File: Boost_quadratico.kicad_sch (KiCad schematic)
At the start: 10 parts

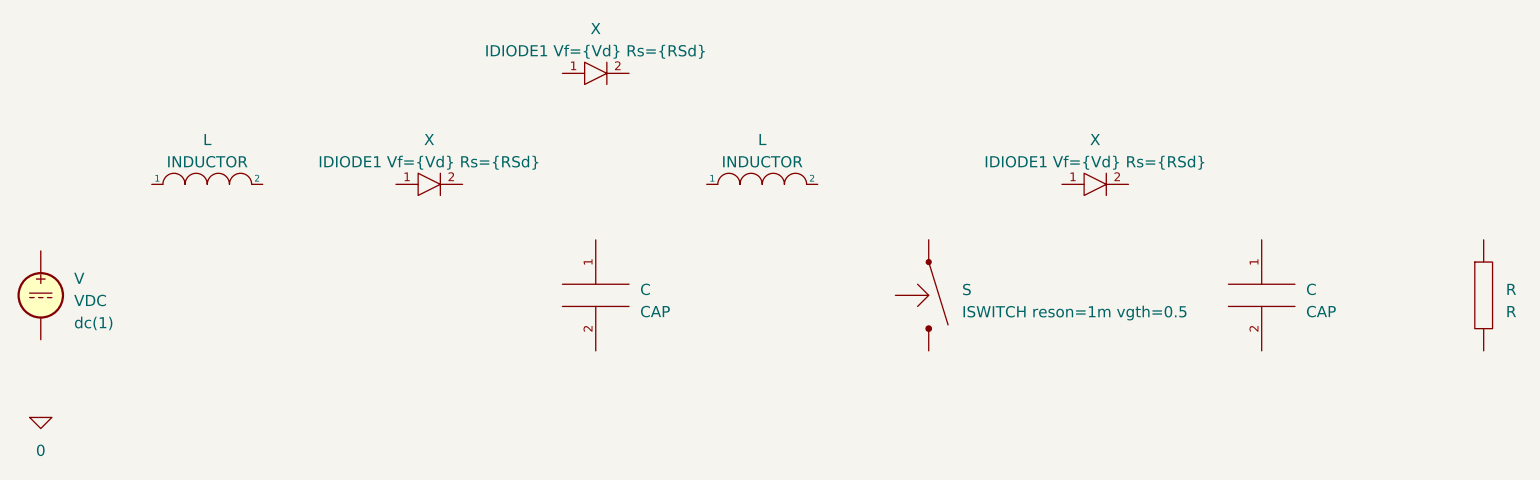
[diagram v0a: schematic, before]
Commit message: Circuito comutado roteado
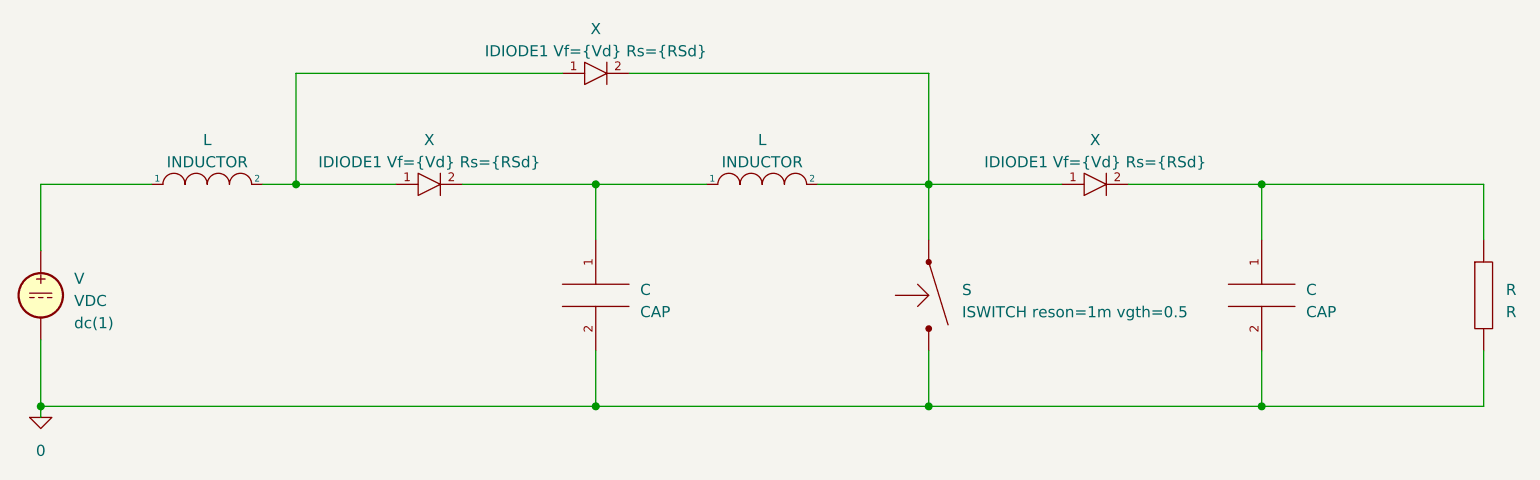
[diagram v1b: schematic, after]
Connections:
- net 0: now also C.2, C.2, R.2, S.3 (S), V.2
- net at V.1: now also L.1
- net at L.1: now also C.1, X.2
- net at L.2: now also S.1 (D), X.1, X.2
- net at X.1: now also L.2, X.1
- net at X.2: now also C.1, R.1
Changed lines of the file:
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@@
 (kicad_sch (version 20220404) (generator eeschema)
   (paper "A4")
+  (junction (at 54.61 88.9) (diameter 0) (color 0 0 0 0)
+  )
+  (junction (at 165.1 114.3) (diameter 0) (color 0 0 0 0)
+  )
+  (junction (at 88.9 114.3) (diameter 0) (color 0 0 0 0)
+  )
+  (junction (at 127 88.9) (diameter 0) (color 0 0 0 0)
+  )
+  (junction (at 88.9 88.9) (diameter 0) (color 0 0 0 0)
+  )
+  (junction (at 165.1 88.9) (diameter 0) (color 0 0 0 0)
+  )
+  (junction (at 127 114.3) (diameter 0) (color 0 0 0 0)
+  )
+  (junction (at 25.4 114.3) (diameter 0) (color 0 0 0 0)
+  )
+  (wire (pts (xy 127 88.9) (xy 142.24 88.9))
+    (stroke (width 0) (type default))
+  )
+  (wire (pts (xy 165.1 114.3) (xy 190.5 114.3))
+    (stroke (width 0) (type default))
+  )
+  (wire (pts (xy 92.71 76.2) (xy 127 76.2))
+    (stroke (width 0) (type default))
+  )
+  (wire (pts (xy 190.5 95.25) (xy 190.5 88.9))
+    (stroke (width 0) (type default))
+  )
+  (wire (pts (xy 114.3 88.9) (xy 127 88.9))
+    (stroke (width 0) (type default))
+  )
+  (wire (pts (xy 25.4 88.9) (xy 38.1 88.9))
+    (stroke (width 0) (type default))
+  )
+  (wire (pts (xy 190.5 107.95) (xy 190.5 114.3))
+    (stroke (width 0) (type default))
+  )
+  (wire (pts (xy 127 114.3) (xy 165.1 114.3))
+    (stroke (width 0) (type default))
+  )
+  (wire (pts (xy 50.8 88.9) (xy 54.61 88.9))
+    (stroke (width 0) (type default))
+  )
+  (wire (pts (xy 73.66 88.9) (xy 88.9 88.9))
+    (stroke (width 0) (type default))
+  )
+  (wire (pts (xy 85.09 76.2) (xy 54.61 76.2))
+    (stroke (width 0) (type default))
+  )
+  (wire (pts (xy 127 114.3) (xy 88.9 114.3))
+    (stroke (width 0) (type default))
+  )
+  (wire (pts (xy 127 107.95) (xy 127 114.3))
+    (stroke (width 0) (type default))
+  )
+  (wire (pts (xy 54.61 88.9) (xy 66.04 88.9))
+    (stroke (width 0) (type default))
+  )
+  (wire (pts (xy 54.61 76.2) (xy 54.61 88.9))
+    (stroke (width 0) (type default))
+  )
+  (wire (pts (xy 190.5 88.9) (xy 165.1 88.9))
+    (stroke (width 0) (type default))
+  )
+  (wire (pts (xy 127 76.2) (xy 127 88.9))
+    (stroke (width 0) (type default))
+  )
+  (wire (pts (xy 149.86 88.9) (xy 165.1 88.9))
+    (stroke (width 0) (type default))
+  )
+  (wire (pts (xy 165.1 107.95) (xy 165.1 114.3))
+    (stroke (width 0) (type default))
+  )
+  (wire (pts (xy 25.4 106.68) (xy 25.4 114.3))
+    (stroke (width 0) (type default))
+  )
+  (wire (pts (xy 25.4 96.52) (xy 25.4 88.9))
+    (stroke (width 0) (type default))
+  )
+  (wire (pts (xy 88.9 88.9) (xy 88.9 95.25))
+    (stroke (width 0) (type default))
+  )
+  (wire (pts (xy 88.9 114.3) (xy 88.9 107.95))
+    (stroke (width 0) (type default))
+  )
+  (wire (pts (xy 88.9 88.9) (xy 101.6 88.9))
+    (stroke (width 0) (type default))
+  )
+  (wire (pts (xy 127 88.9) (xy 127 95.25))
+    (stroke (width 0) (type default))
+  )
+  (wire (pts (xy 25.4 114.3) (xy 25.4 115.57))
+    (stroke (width 0) (type default))
+  )
+  (wire (pts (xy 165.1 88.9) (xy 165.1 95.25))
+    (stroke (width 0) (type default))
+  )
+  (wire (pts (xy 25.4 114.3) (xy 88.9 114.3))
+    (stroke (width 0) (type default))
+  )
   (symbol (lib_id "Simulation_SPICE:VDC") (at 25.4 101.6 0) (unit 1)
     (in_bom yes) (on_board yes) (fields_autoplaced)

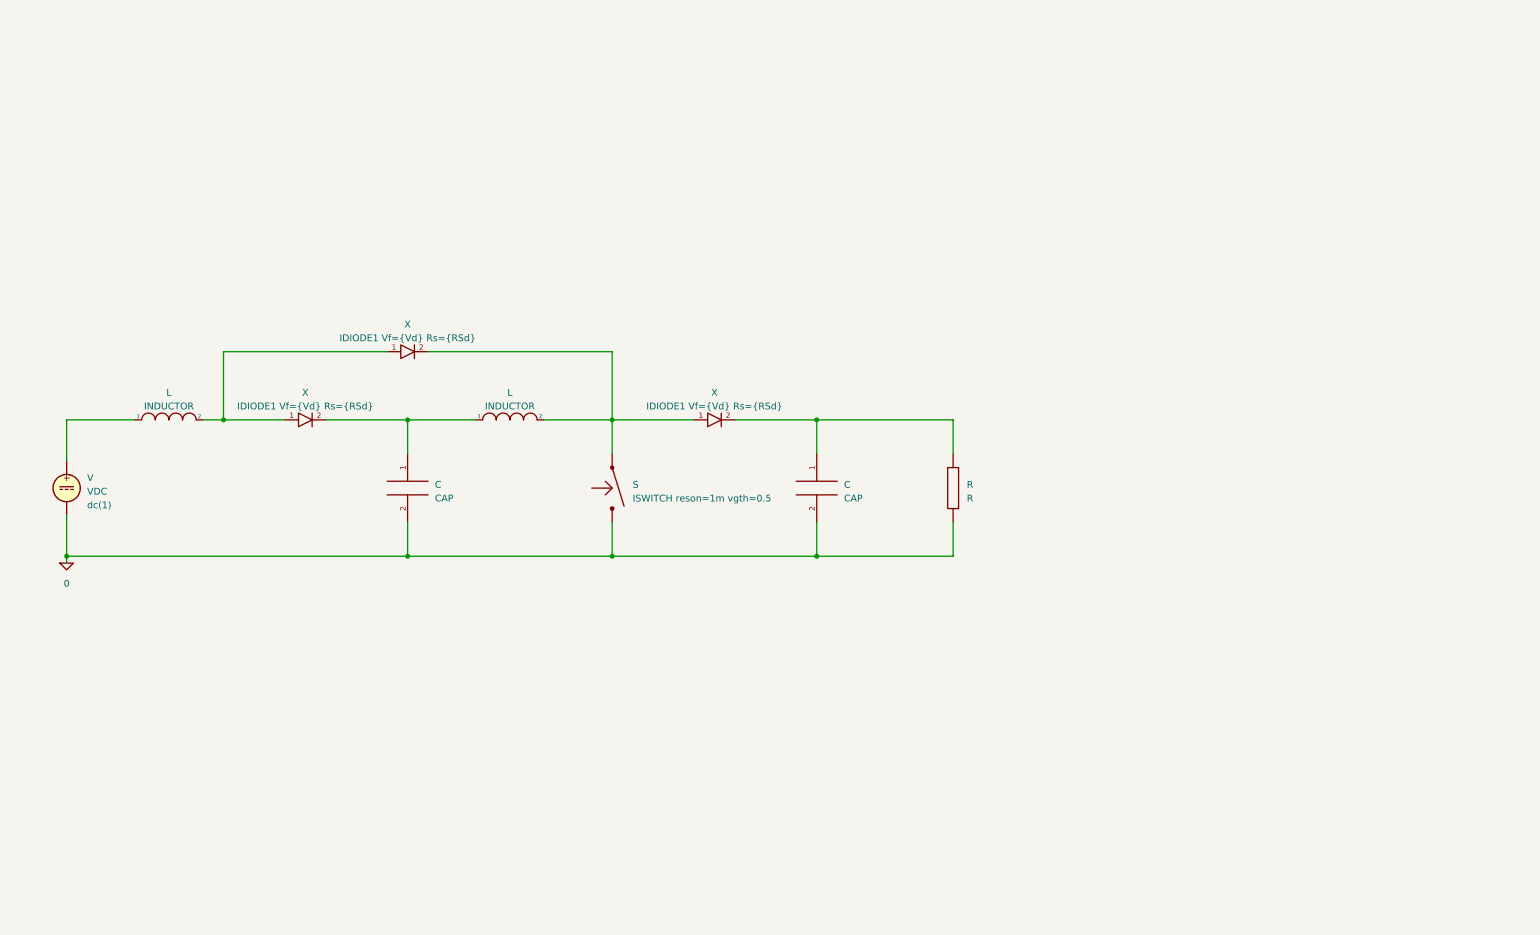
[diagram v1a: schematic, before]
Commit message: Modelo médio PWMgst
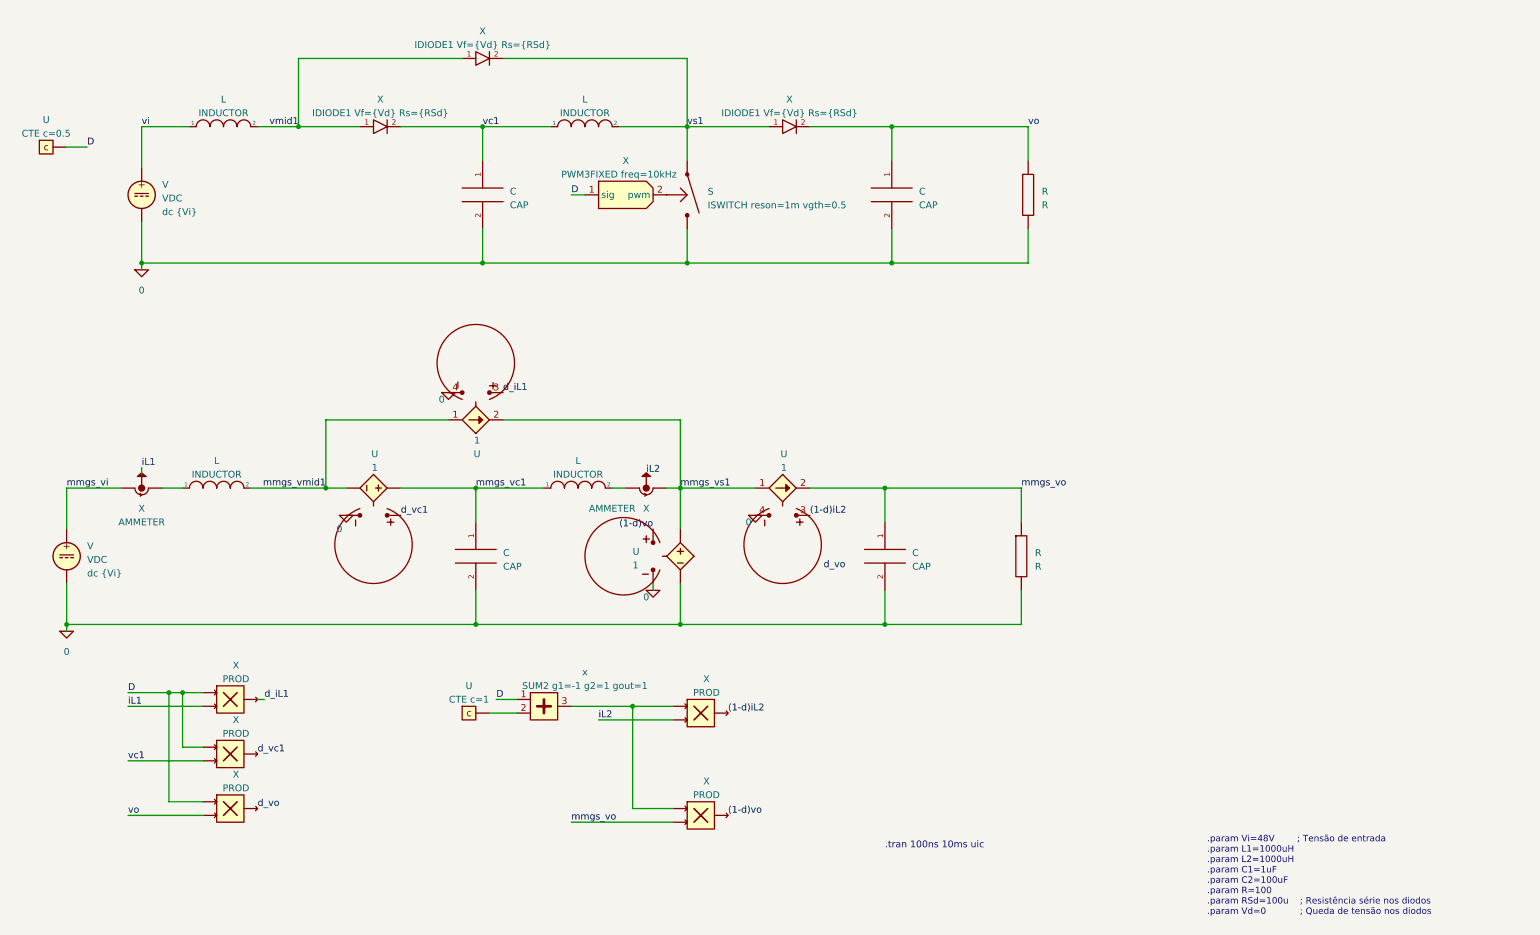
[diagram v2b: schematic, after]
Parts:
- added C (x2): CAP, symbol pspice:CAP
- added L (x2): INDUCTOR, symbol pspice:INDUCTOR
- added R: R, symbol pspice:R
- added U (x2): VCCS, symbol power electronics:VCCS
- added U (x2): VCVS, symbol power electronics:VCVS
- added V: VDC, symbol Simulation_SPICE:VDC
- added X (x5): product, symbol Signal Processing:product
- added X: PWM3_FIXED, symbol power electronics:PWM3_FIXED
- added X (x2): Ammeter Compact, symbol Signal Processing:Ammeter Compact
- added x: sum2, symbol Signal Processing:sum2
- V: Spice_Model dc(1) -> dc {Vi}
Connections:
- net 0: now also C.2, C.2, R.2, U.2, U.4, U.4, U.4, U.4, V.2
- net vi: now reaches L.1, V.1
- net vc1: now reaches C.1, L.1, X.2
- net vc1: now also X.2
- net vs1: now reaches L.2, S.1 (D), X.1, X.2
- net vmid1: now reaches L.2, X.1, X.1
- net at S.2 (G): now also X.2 (pwm)
- net vo: now reaches C.1, R.1, X.2
- net vo: now also X.2
- new net: X.1, X.1, x.3
- new net: L.2, X.1
- new net: L.1, X.2
- new net (1-d)iL2: U.3, X.3
- new net (1-d)vo: U.3, X.3
- new net D: X.1, X.1, X.1, X.1 (sig), x.1
- new net d_iL1: U.3, X.3
- new net d_vc1: U.3, X.3
- new net d_vo: X.3
- new net iL1: X.2, X.3
- new net iL2: X.2, X.3
- new net mmgs_vc1: C.1, L.1, U.1
- new net mmgs_vi: V.1, X.1
- new net mmgs_vmid1: L.2, U.1, U.2
- new net mmgs_vo: C.1, R.1, U.2, X.2
- new net mmgs_vs1: U.1, U.1, U.2, X.2
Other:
- note added: ".param Vi=48V ; Tensão de entrada .param L1=1000uH .param L2=1000uH .param C1=1uF .param C2=100uF .param R=100 .param RSd=100u ; Resistência série nos diodos .param Vd=0 ; Queda de tensão nos diodos"
- note added: ".tran 100ns 10ms uic"
- company: (none) -> INEP - UFSC
- title: (none) -> Conversor Boost Quadrático
- moved on the sheet: C, L, R, S, V, X

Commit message: Modelo médio feito, mas oscilando demais
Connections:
- net (1-d)iL2: no longer U.3
- net (1-d)vo: no longer U.3
- net 0: now also U.2, U.3; no longer U.2, U.4
- net d_iL1: now also U.4
- net d_vo: now also U.3
- net mmgs_vo: now also U.1; no longer U.2
- net mmgs_vs1: now also U.2; no longer U.1
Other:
- moved on the sheet: U
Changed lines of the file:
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@@
+    (stroke (width 0) (type default))
+  )
+  (wire (pts (xy 68.58 34.29) (xy 80.01 34.29))
+    (stroke (width 0) (type default))
+  )
+  (wire (pts (xy 68.58 21.59) (xy 68.58 34.29))
+    (stroke (width 0) (type default))
+  )
+  (wire (pts (xy 104.14 143.51) (xy 109.22 143.51))
+    (stroke (width 0) (type default))
+  )
+  (wire (pts (xy 50.8 160.02) (xy 44.45 160.02))
+    (stroke (width 0) (type default))
+  )
+  (wire (pts (xy 36.83 142.24) (xy 50.8 142.24))
+    (stroke (width 0) (type default))
+  )
+  (wire (pts (xy 204.47 34.29) (xy 179.07 34.29))
+    (stroke (width 0) (type default))
+  )
+  (wire (pts (xy 177.8 101.6) (xy 177.8 107.95))
+    (stroke (width 0) (type default))
+  )
+  (wire (pts (xy 25.4 127) (xy 101.6 127))
+    (stroke (width 0) (type default))
+  )
+  (wire (pts (xy 140.97 21.59) (xy 140.97 34.29))
+    (stroke (width 0) (type default))
+  )
+  (wire (pts (xy 163.83 34.29) (xy 179.07 34.29))
+    (stroke (width 0) (type default))
+  )
+  (wire (pts (xy 36.83 152.4) (xy 50.8 152.4))
     (stroke (width 0) (type default))
   )
   (wire (pts (xy 134.62 119.38) (xy 134.62 120.65))
-    (stroke (width 0) (type default))
-  )
-  (wire (pts (xy 68.58 34.29) (xy 80.01 34.29))
-    (stroke (width 0) (type default))
-  )
-  (wire (pts (xy 68.58 21.59) (xy 68.58 34.29))
-    (stroke (width 0) (type default))
-  )
-  (wire (pts (xy 104.14 143.51) (xy 109.22 143.51))
-    (stroke (width 0) (type default))
-  )
-  (wire (pts (xy 50.8 160.02) (xy 44.45 160.02))
-    (stroke (width 0) (type default))
-  )
-  (wire (pts (xy 36.83 142.24) (xy 50.8 142.24))
-    (stroke (width 0) (type default))
-  )
-  (wire (pts (xy 204.47 34.29) (xy 179.07 34.29))
-    (stroke (width 0) (type default))
-  )
-  (wire (pts (xy 177.8 101.6) (xy 177.8 107.95))
-    (stroke (width 0) (type default))
-  )
-  (wire (pts (xy 25.4 127) (xy 101.6 127))
-    (stroke (width 0) (type default))
-  )
-  (wire (pts (xy 140.97 21.59) (xy 140.97 34.29))
-    (stroke (width 0) (type default))
-  )
-  (wire (pts (xy 163.83 34.29) (xy 179.07 34.29))
-    (stroke (width 0) (type default))
-  )
-  (wire (pts (xy 36.83 152.4) (xy 50.8 152.4))
     (stroke (width 0) (type default))
   )
@@
     (effects (font (size 1.27 1.27)) (justify left bottom))
   )
-  (label "(1-d)vo" (at 134.62 109.22 0) (fields_autoplaced)
-    (effects (font (size 1.27 1.27)) (justify right bottom))
+  (label "d_vo" (at 163.83 96.52 0) (fields_autoplaced)
+    (effects (font (size 1.27 1.27)) (justify left bottom))
   )
   (label "d_iL1" (at 106.68 83.82 0) (fields_autoplaced)
@@
     (effects (font (size 1.27 1.27)) (justify left bottom))
   )
-  (label "(1-d)iL2" (at 163.83 106.68 0) (fields_autoplaced)
+  (label "d_iL1" (at 134.62 109.22 0) (fields_autoplaced)
     (effects (font (size 1.27 1.27)) (justify left bottom))
   )
@@
     (pin "2")
   )
-  (symbol (lib_id "power electronics:VCVS") (at 139.7 114.3 0) (mirror y) (unit 1)
+  (symbol (lib_id "power electronics:VCVS") (at 158.75 101.6 270) (mirror x) (unit 1)
     (in_bom no) (on_board no)
     (default_instance (reference "U") (unit 1) (value "VCVS") (footprint ""))
-    (property "Reference" "U" (id 0) (at 130.81 113.4297 0)
+    (property "Reference" "U" (id 0) (at 159.6203 92.71 0)
       (effects (font (size 1.27 1.27)) (justify right))
     )
-    (property "Value" "VCVS" (id 1) (at 139.7 132.08 0)
-      (effects (font (size 1.27 1.27)) hide)
-    )
-    (property "Footprint" "" (id 2) (at 139.7 129.54 0)
-      (effects (font (size 1.27 1.27)) hide)
-    )
-    (property "Datasheet" "" (id 3) (at 139.7 129.54 0)
-      (effects (font (size 1.27 1.27)) hide)
-    )
-    (property "Spice_Primitive" "E" (id 4) (at 139.7 127 0)
-      (effects (font (size 1.27 1.27)) hide)
-    )
-    (property "Spice_Model" "1" (id 5) (at 130.81 115.9697 0)
+    (property "Value" "VCVS" (id 1) (at 140.97 101.6 0)
+      (effects (font (size 1.27 1.27)) hide)
+    )
+    (property "Footprint" "" (id 2) (at 143.51 101.6 0)
+      (effects (font (size 1.27 1.27)) hide)
+    )
+    (property "Datasheet" "" (id 3) (at 143.51 101.6 0)
+      (effects (font (size 1.27 1.27)) hide)
+    )
+    (property "Spice_Primitive" "E" (id 4) (at 146.05 101.6 0)
+      (effects (font (size 1.27 1.27)) hide)
+    )
+    (property "Spice_Model" "1" (id 5) (at 157.0803 92.71 0)
       (effects (font (size 1.27 1.27)) (justify right))
     )
-    (property "Spice_Netlist_Enabled" "Y" (id 6) (at 139.7 129.54 0)
+    (property "Spice_Netlist_Enabled" "Y" (id 6) (at 143.51 101.6 0)
       (effects (font (size 1.27 1.27)) hide)
     )
@@
     (pin "3")
   )
-  (symbol (lib_id "power electronics:VCCS") (at 158.75 101.6 270) (unit 1)
+  (symbol (lib_id "power electronics:VCCS") (at 139.7 114.3 180) (unit 1)
     (in_bom no) (on_board no) (fields_autoplaced)
     (default_instance (reference "U") (unit 1) (value "VCCS") (footprint ""))
-    (property "Reference" "U" (id 0) (at 158.9853 95.25 90)
-      (effects (font (size 1.27 1.27)))
-    )
-    (property "Value" "VCCS" (id 1) (at 139.7 101.6 0)
-      (effects (font (size 1.27 1.27)) hide)
-    )
-    (property "Footprint" "" (id 2) (at 143.51 101.6 0)
-      (effects (font (size 1.27 1.27)) hide)
-    )
-    (property "Datasheet" "" (id 3) (at 143.51 101.6 0)
-      (effects (font (size 1.27 1.27)) hide)
-    )
-    (property "Spice_Primitive" "G" (id 4) (at 144.78 101.6 0)
-      (effects (font (size 1.27 1.27)) hide)
-    )
-    (property "Spice_Model" "1" (id 5) (at 158.9853 97.79 90)
-      (effects (font (size 1.27 1.27)))
-    )
-    (property "Spice_Netlist_Enabled" "Y" (id 6) (at 142.24 101.6 0)
+    (property "Reference" "U" (id 0) (at 143.51 113.9003 0)
+      (effects (font (size 1.27 1.27)) (justify right))
+    )
+    (property "Value" "VCCS" (id 1) (at 139.7 95.25 0)
+      (effects (font (size 1.27 1.27)) hide)
+    )
+    (property "Footprint" "" (id 2) (at 139.7 99.06 0)
+      (effects (font (size 1.27 1.27)) hide)
+    )
+    (property "Datasheet" "" (id 3) (at 139.7 99.06 0)
+      (effects (font (size 1.27 1.27)) hide)
+    )
+    (property "Spice_Primitive" "G" (id 4) (at 139.7 100.33 0)
+      (effects (font (size 1.27 1.27)) hide)
+    )
+    (property "Spice_Model" "1" (id 5) (at 143.51 116.4403 0)
+      (effects (font (size 1.27 1.27)) (justify right))
+    )
+    (property "Spice_Netlist_Enabled" "Y" (id 6) (at 139.7 97.79 0)
       (effects (font (size 1.27 1.27)) hide)
     )
@@
     (pin "3")
   )
-  (symbol (lib_id "pspice:0") (at 153.67 106.68 0) (unit 1)
+  (symbol (lib_id "pspice:0") (at 153.67 96.52 0) (unit 1)
     (in_bom yes) (on_board yes)
     (default_instance (reference "#GND") (unit 1) (value "0") (footprint ""))
-    (property "Reference" "#GND" (id 0) (at 153.67 109.22 0)
-      (effects (font (size 1.27 1.27)) hide)
-    )
-    (property "Value" "0" (id 1) (at 152.4 107.95 0)
-      (effects (font (size 1.27 1.27)))
-    )
-    (property "Footprint" "" (id 2) (at 153.67 106.68 0)
-      (effects (font (size 1.27 1.27)) hide)
-    )
-    (property "Datasheet" "~" (id 3) (at 153.67 106.68 0)
-      (effects (font (size 1.27 1.27)) hide)
-    )
+    (property "Reference" "#GND" (id 0) (at 153.67 99.06 0)
+      (effects (font (size 1.27 1.27)) hide)
+    )
+    (property "Value" "0" (id 1) (at 152.4 97.79 0)
+      (effects (font (size 1.27 1.27)))
+    )
+    (property "Footprint" "" (id 2) (at 153.67 96.52 0)
+      (effects (font (size 1.27 1.27)) hide)
+    )
+    (property "Datasheet" "~" (id 3) (at 153.67 96.52 0)
+      (effects (font (size 1.27 1.27)) hide)
+    )
